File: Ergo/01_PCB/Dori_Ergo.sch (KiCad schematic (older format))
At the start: 208 parts, among them J1 TYPE-C-31-M12_13, J2 AVR-ISP-6_mod, J3 4PIN, J4 4PIN, J5 TYPE-C-31-M12_13, J6 AVR-ISP-6_mod, K1 KEYSW, K10 KEYSW, K11 KEYSW, K12 KEYSW, K13 KEYSW, K14 KEYSW, K15 KEYSW, K16 KEYSW, K17 KEYSW, K18 KEYSW, K19 KEYSW, K2 KEYSW, K20 KEYSW, K21 KEYSW, K22 KEYSW, K23 KEYSW, K24 KEYSW, K25 KEYSW, K26 KEYSW, K27 KEYSW, K28 KEYSW, K29 KEYSW, K3 KEYSW, K30 KEYSW, K31 KEYSW, K32 KEYSW, K33 KEYSW, K34 KEYSW, K35 KEYSW, K36 KEYSW, K37 KEYSW, K38 KEYSW, K39 KEYSW, K4 KEYSW, K40 KEYSW, K41 KEYSW, K42 KEYSW, K43 KEYSW, K44 KEYSW, K45 KEYSW, K46 KEYSW, K47 KEYSW, K48 KEYSW, K49 KEYSW, K5 KEYSW, K50 KEYSW, K51 KEYSW, K52 KEYSW, K53 KEYSW, K54 KEYSW, K55 KEYSW, K56 KEYSW, K6 KEYSW, K7 KEYSW, K8 KEYSW, K9 KEYSW, SW1 SW_PUSH, SW10 Rotary_Encoder_Switch, SW2 SW_PUSH, SW3 Rotary_Encoder_Switch, SW4 Rotary_Encoder_Switch, SW5 Rotary_Encoder_Switch, SW6 Rotary_Encoder_Switch, SW7 Rotary_Encoder_Switch, SW8 Rotary_Encoder_Switch, SW9 Rotary_Encoder_Switch, U1 ATMEGA32U4, U10 HOLE, U11 HOLE, U12 ATMEGA32U4, U13 HOLE, U14 HOLE, U15 HOLE, U16 HOLE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

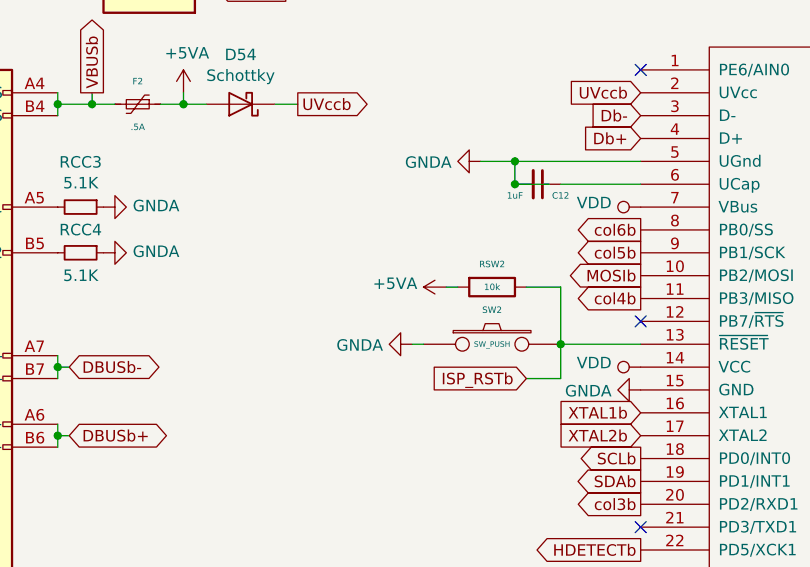
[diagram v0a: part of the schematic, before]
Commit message: Ergo routing
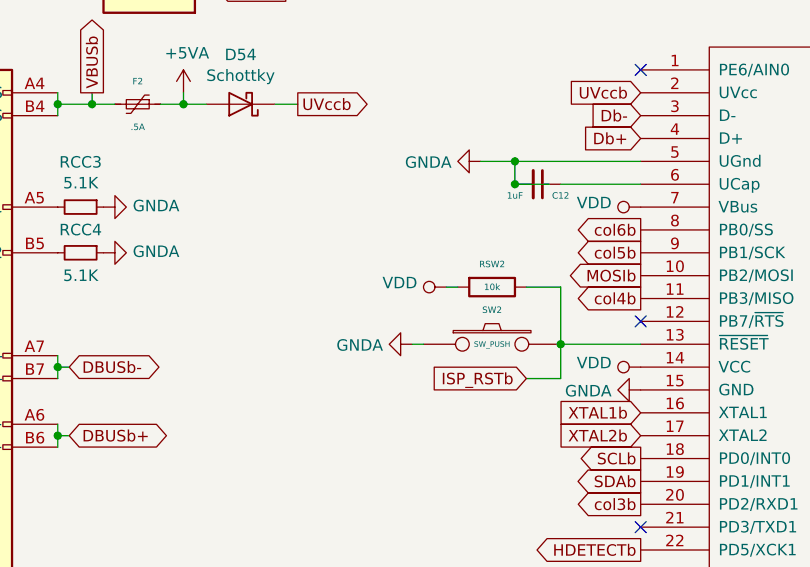
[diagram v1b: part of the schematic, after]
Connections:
- net +5VA: no longer RSW2.2
- net VDD: now also RSW2.2
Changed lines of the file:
@@
-$EndComp
-$Comp
-L power:+5VA #PWR0149
-U 1 1 5FD8BF6F
-P 16600 8100
-F 0 "#PWR0149" H 16600 7950 50  0001 C CNN
-F 1 "+5VA" V 16615 8227 50  0000 L CNN
-F 2 "" H 16600 8100 50  0001 C CNN
-F 3 "" H 16600 8100 50  0001 C CNN
-	1    16600 8100
-	0    -1   -1   0
 $EndComp
 $Comp
@@
 Text GLabel 4800 11950 0    50   Input ~ 0
 UVcca
+$Comp
+L power:VDD #PWR0120
+U 1 1 5F3A8DE0
+P 16600 8100
+F 0 "#PWR0120" H 16600 7950 50  0001 C CNN
+F 1 "VDD" V 16618 8227 50  0000 L CNN
+F 2 "" H 16600 8100 50  0001 C CNN
+F 3 "" H 16600 8100 50  0001 C CNN
+	1    16600 8100
+	0    -1   -1   0
+$EndComp
 $EndSCHEMATC

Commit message: Finished routing Ergo
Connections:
- net UVcca is gone; now on net +5V: C5.1, D53.2 (A), F1.1, R4.2, U1.2 (UVcc)
- net +5V: now also J2.2 (VCC), U1.7 (VBus)
- net +5VA: now also C11.1, J6.2 (VCC), U12.2 (UVcc), U12.7 (VBus)
- net Enc2a: now also U12.27 (T0/PD7); no longer U12.31 (PC6)
- net Enc2b: now also U12.28 (PB4); no longer U12.30 (PB6)
- net VCC: no longer J2.2 (VCC), U1.7 (VBus)
- net VDD: now also D54.1 (K); no longer C11.1, J6.2 (VCC), U12.7 (VBus)
- net col0b: now also U12.25 (ICP1/PD4); no longer U12.27 (T0/PD7)
- net col1b: now also U12.37 (PF6); no longer U12.28 (PB4)
- net col2b: now also U12.8 (PB0/SS); no longer U12.29 (PB5)
- net col3b: now also U12.41 (PF0); no longer U12.20 (PD2/RXD1)
- net col6b: now also U12.40 (PF1); no longer U12.8 (PB0/SS)
- net row0b: now also U12.1 (PE6/AIN0); no longer U12.36 (PF7)
- net row1b: now also U12.42 (AREF); no longer U12.37 (PF6)
- net row2b: now also U12.29 (PB5); no longer U12.26 (T1/PD6)
- net row3b: now also U12.12 (PB7/~RTS); no longer U12.25 (ICP1/PD4)
- removed net UVccb: D54.1 (K), U12.2 (UVcc)
- no-connect marks 11 -> 5
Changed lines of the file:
@@
 $EndComp
 $Comp
-L power:VCC #PWR0107
-U 1 1 5DF6EB55
-P 7450 8100
-F 0 "#PWR0107" H 7450 7950 50  0001 C CNN
-F 1 "VCC" V 7468 8227 50  0000 L CNN
-F 2 "" H 7450 8100 50  0001 C CNN
-F 3 "" H 7450 8100 50  0001 C CNN
-	1    7450 8100
-	0    -1   -1   0
-$EndComp
-$Comp
 L power:VCC #PWR0110
 U 1 1 5DF6F7F4
@@
 	0    1    1    0
 $EndComp
-$Comp
-L power:VCC #PWR0125
-U 1 1 5E2877E3
-P 8600 10550
-F 0 "#PWR0125" H 8600 10400 50  0001 C CNN
-F 1 "VCC" V 8617 10678 50  0000 L CNN
-F 2 "" H 8600 10550 50  0001 C CNN
-F 3 "" H 8600 10550 50  0001 C CNN
-	1    8600 10550
-	0    1    1    0
-$EndComp
 Text Notes 6350 11500 0    50   ~ 0
 ESD Protection
@@
 Text GLabel 14950 8450 2    50   BiDi ~ 0
 DBUSb-
-Text GLabel 19600 7850 2    50   Output ~ 0
+Text GLabel 19600 7350 2    50   Output ~ 0
 row1b
-Text GLabel 19600 8750 2    50   Output ~ 0
+Text GLabel 19600 7850 2    50   Output ~ 0
 col1b
-Text GLabel 19600 8650 2    50   Output ~ 0
+Text GLabel 17450 7850 0    50   Output ~ 0
 col2b
-Text GLabel 19600 7950 2    50   Output ~ 0
+Text GLabel 17450 7150 0    50   Output ~ 0
 row0b
 Text GLabel 17450 8150 0    50   Output ~ 0
@@
 Text GLabel 17450 7950 0    50   Output ~ 0
 col5b
-NoConn ~ 19600 7350
 $Comp
 L Device:Polyfuse_Small F2
@@
 Text GLabel 17450 7350 0    50   Input ~ 0
 Db-
-Text GLabel 17450 9050 0    50   Output ~ 0
+Text GLabel 19600 7450 2    50   Output ~ 0
 col3b
 NoConn ~ 19600 8350
-Text GLabel 19600 9050 2    50   Output ~ 0
+Text GLabel 17450 8250 0    50   Output ~ 0
 row3b
 $Comp
@@
 Wire Notes Line
 	14550 12150 14550 11700
-Text GLabel 19600 8850 2    50   Output ~ 0
+Text GLabel 19600 9050 2    50   Output ~ 0
 col0b
 Text GLabel 17450 8850 0    50   Output ~ 0
@@
 Connection ~ 2400 3950
 $Comp
-L power:VDD #PWR0138
-U 1 1 604F88A2
-P 17450 7750
-F 0 "#PWR0138" H 17450 7600 50  0001 C CNN
-F 1 "VDD" V 17468 7877 50  0000 L CNN
-F 2 "" H 17450 7750 50  0001 C CNN
-F 3 "" H 17450 7750 50  0001 C CNN
-	1    17450 7750
-	0    -1   -1   0
-$EndComp
-$Comp
 L power:VDD #PWR0139
 U 1 1 604F9EB0
@@
 	0    1    1    0
 $EndComp
-Text GLabel 19600 8950 2    50   Output ~ 0
-row2b
-Text GLabel 19600 8550 2    50   Output ~ 0
+Text GLabel 19600 8750 2    50   Output ~ 0
 Enc2b
-Text GLabel 19600 8450 2    50   Output ~ 0
+Text GLabel 19600 8850 2    50   Output ~ 0
 Enc2a
 $Comp
@@
 Wire Wire Line
 	18300 12000 18100 12000
-Connection ~ 18300 12000
 Wire Wire Line
 	18100 12000 17900 12000
@@
 Connection ~ 17900 12000
 Connection ~ 17700 12000
-Wire Wire Line
-	18500 12000 18300 12000
 $Comp
 L Device:C_Small C7
@@
 $EndComp
 $Comp
-L power:VDD #PWR0158
-U 1 1 6050CEE0
-P 18750 10550
-F 0 "#PWR0158" H 18750 10400 50  0001 C CNN
-F 1 "VDD" V 18767 10678 50  0000 L CNN
-F 2 "" H 18750 10550 50  0001 C CNN
-F 3 "" H 18750 10550 50  0001 C CNN
-	1    18750 10550
-	0    1    1    0
-$EndComp
-$Comp
 L power:GNDA #PWR0157
 U 1 1 6050B96B
@@
 L power:+5V #PWR0135
 U 1 1 5FC4DB27
-P 6000 7250
-F 0 "#PWR0135" H 6000 7100 50  0001 C CNN
-F 1 "+5V" H 6015 7423 50  0000 C CNN
-F 2 "" H 6000 7250 50  0001 C CNN
-F 3 "" H 6000 7250 50  0001 C CNN
-	1    6000 7250
+P 5450 7600
+F 0 "#PWR0135" H 5450 7450 50  0001 C CNN
+F 1 "+5V" H 5465 7773 50  0000 C CNN
+F 2 "" H 5450 7600 50  0001 C CNN
+F 3 "" H 5450 7600 50  0001 C CNN
+	1    5450 7600
 	1    0    0    -1
 $EndComp
@@
 	0    -1   -1   0
 $EndComp
-Text GLabel 17450 7850 0    50   Output ~ 0
+Text GLabel 19600 7550 2    50   Output ~ 0
 col6b
 Text GLabel 19600 7750 2    50   Output ~ 0
@@
 Wire Notes Line
 	11150 3800 12700 3800
-NoConn ~ 17450 8250
-NoConn ~ 19600 7450
-NoConn ~ 19600 7550
-NoConn ~ 17450 7150
-NoConn ~ 17450 9150
-Text GLabel 5450 7600 1    50   Output ~ 0
-UVcca
-Text GLabel 15950 7300 2    50   Output ~ 0
-UVccb
-Text GLabel 17450 7250 0    50   Input ~ 0
-UVccb
 Wire Wire Line
 	8200 5350 7350 5350
@@
 	1    0    0    -1
 $EndComp
-Text GLabel 7450 7600 0    50   Input ~ 0
-UVcca
-Text GLabel 8250 12000 1    50   Output ~ 0
-UVcca
-Text GLabel 4800 11950 0    50   Input ~ 0
-UVcca
 $Comp
 L power:VDD #PWR0120
@@
 	0    -1   -1   0
 $EndComp
+Text GLabel 19600 8650 2    50   Output ~ 0
+row2b
+$Comp
+L power:+5V #PWR0107
+U 1 1 5F53C25B
+P 7450 7600
+F 0 "#PWR0107" H 7450 7450 50  0001 C CNN
+F 1 "+5V" V 7465 7728 50  0000 L CNN
+F 2 "" H 7450 7600 50  0001 C CNN
+F 3 "" H 7450 7600 50  0001 C CNN
+	1    7450 7600
+	0    -1   -1   0
+$EndComp
+$Comp
+L power:+5V #PWR0125
+U 1 1 5F53D8FF
+P 7450 8100
+F 0 "#PWR0125" H 7450 7950 50  0001 C CNN
+F 1 "+5V" V 7465 8228 50  0000 L CNN
+F 2 "" H 7450 8100 50  0001 C CNN
+F 3 "" H 7450 8100 50  0001 C CNN
+	1    7450 8100
+	0    -1   -1   0
+$EndComp
+$Comp
+L power:+5V #PWR0126
+U 1 1 5F53EF8E
+P 4800 11950
+F 0 "#PWR0126" H 4800 11800 50  0001 C CNN
+F 1 "+5V" V 4815 12078 50  0000 L CNN
+F 2 "" H 4800 11950 50  0001 C CNN
+F 3 "" H 4800 11950 50  0001 C CNN
+	1    4800 11950
+	0    -1   -1   0
+$EndComp
+$Comp
+L power:+5V #PWR0137
+U 1 1 5F5405EB
+P 8250 12000
+F 0 "#PWR0137" H 8250 11850 50  0001 C CNN
+F 1 "+5V" H 8265 12173 50  0000 C CNN
+F 2 "" H 8250 12000 50  0001 C CNN
+F 3 "" H 8250 12000 50  0001 C CNN
+	1    8250 12000
+	1    0    0    -1
+$EndComp
+$Comp
+L power:+5VA #PWR0138
+U 1 1 5F54326C
+P 17450 7250
+F 0 "#PWR0138" H 17450 7100 50  0001 C CNN
+F 1 "+5VA" V 17465 7377 50  0000 L CNN
+F 2 "" H 17450 7250 50  0001 C CNN
+F 3 "" H 17450 7250 50  0001 C CNN
+	1    17450 7250
+	0    -1   -1   0
+$EndComp
+$Comp
+L power:+5VA #PWR0141
+U 1 1 5F5448E2
+P 17450 7750
+F 0 "#PWR0141" H 17450 7600 50  0001 C CNN
+F 1 "+5VA" V 17465 7877 50  0000 L CNN
+F 2 "" H 17450 7750 50  0001 C CNN
+F 3 "" H 17450 7750 50  0001 C CNN
+	1    17450 7750
+	0    -1   -1   0
+$EndComp
+$Comp
+L power:VDD #PWR0149
+U 1 1 5F550A69
+P 15950 7300
+F 0 "#PWR0149" H 15950 7150 50  0001 C CNN
+F 1 "VDD" V 15967 7428 50  0000 L CNN
+F 2 "" H 15950 7300 50  0001 C CNN
+F 3 "" H 15950 7300 50  0001 C CNN
+	1    15950 7300
+	0    1    1    0
+$EndComp
+$Comp
+L power:+5V #PWR0175
+U 1 1 5F61E9FB
+P 8600 10550
+F 0 "#PWR0175" H 8600 10400 50  0001 C CNN
+F 1 "+5V" V 8615 10678 50  0000 L CNN
+F 2 "" H 8600 10550 50  0001 C CNN
+F 3 "" H 8600 10550 50  0001 C CNN
+	1    8600 10550
+	0    1    1    0
+$EndComp
+$Comp
+L power:+5VA #PWR0158
+U 1 1 5F66ADA7
+P 18750 10550
+F 0 "#PWR0158" H 18750 10400 50  0001 C CNN
+F 1 "+5VA" V 18765 10678 50  0000 L CNN
+F 2 "" H 18750 10550 50  0001 C CNN
+F 3 "" H 18750 10550 50  0001 C CNN
+	1    18750 10550
+	0    1    1    0
+$EndComp
+$Comp
+L power:+5VA #PWR0176
+U 1 1 5F72CE9B
+P 18500 12000
+F 0 "#PWR0176" H 18500 11850 50  0001 C CNN
+F 1 "+5VA" H 18515 12173 50  0000 C CNN
+F 2 "" H 18500 12000 50  0001 C CNN
+F 3 "" H 18500 12000 50  0001 C CNN
+	1    18500 12000
+	1    0    0    -1
+$EndComp
 $EndSCHEMATC
